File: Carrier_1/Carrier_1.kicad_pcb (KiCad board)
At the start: 2 copper layers, 20 x 32 mm, 3 parts, among them J1 Chubut_2 connector, U1 LGAD_2_pad

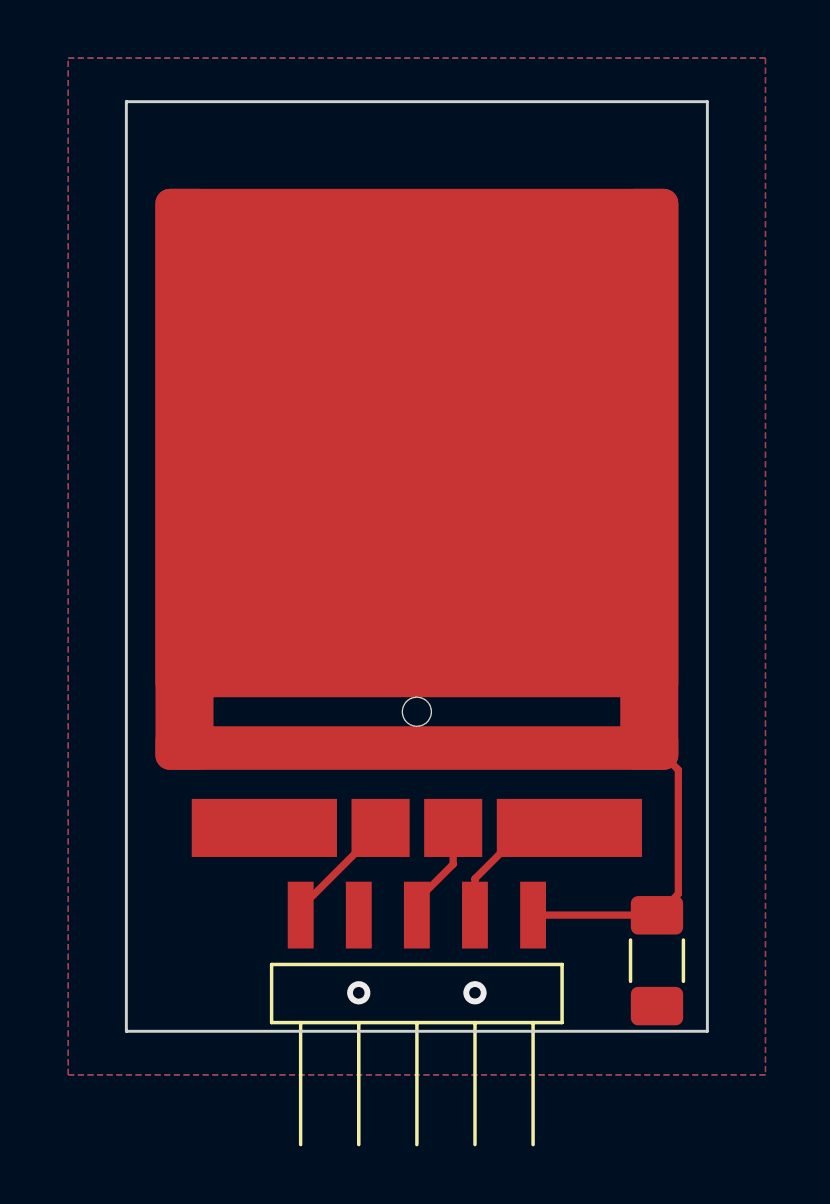
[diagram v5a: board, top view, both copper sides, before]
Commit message: Design with spring loaded pins
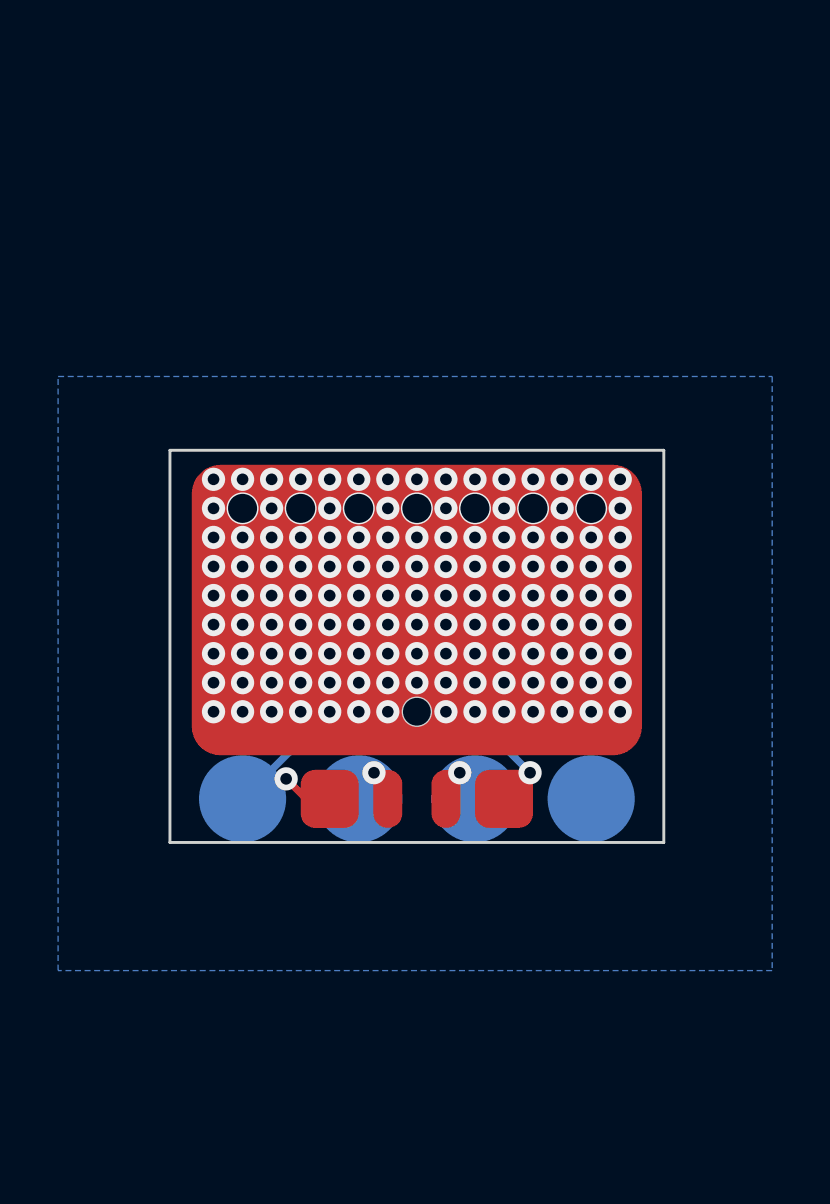
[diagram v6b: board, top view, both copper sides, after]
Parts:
- removed C1: 1n, Capacitor_SMD:C_1206_3216Metric_Pad1.33x1.80mm_HandSolder
- added J2: CH2, chubut:MILL-MAX_0965-0-15-20-80-14-11-0_contact, B.Cu at (2.00, 3.00)
- added J3: HV, chubut:MILL-MAX_0965-0-15-20-80-14-11-0_contact, B.Cu at (6.00, 3.00)
- added J4: GND, chubut:MILL-MAX_0965-0-15-20-80-14-11-0_contact, B.Cu at (-6.00, 3.00)
- J1: value Chubut_2 connector -> CH1; footprint chubut:M22-5330505 -> chubut:MILL-MAX_0965-0-15-20-80-14-11-0_contact; moved to B.Cu
- moved J1 4.47 mm to (-2.00, 3.00), turned to 180 degrees
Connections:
- U1 pad 1: Net-(C1-Pad1) -> /HV
- U1 pad 3: Net-(J1-Pad3) -> Net-(J2-Pad1)
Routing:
- net Net-(C1-Pad1): track 18.9 -> 0.00 mm
- net GND: track 5.22 -> 14.6 mm
- net Net-(J1-Pad3): track 3.52 -> 0.00 mm
- net Net-(J2-Pad1): track 0.00 -> 2.22 mm, vias 0 -> 1
- net Net-(J1-Pad1): track 4.14 -> 2.22 mm, vias 0 -> 1
- net /HV: vias 0 -> 134
- added copper zone on B.Cu, net /HV
- removed copper zone on B.Cu, net GND
- removed copper zone on F.Cu, net GND
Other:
- board size 20 x 32 mm -> 17 x 13.5 mm

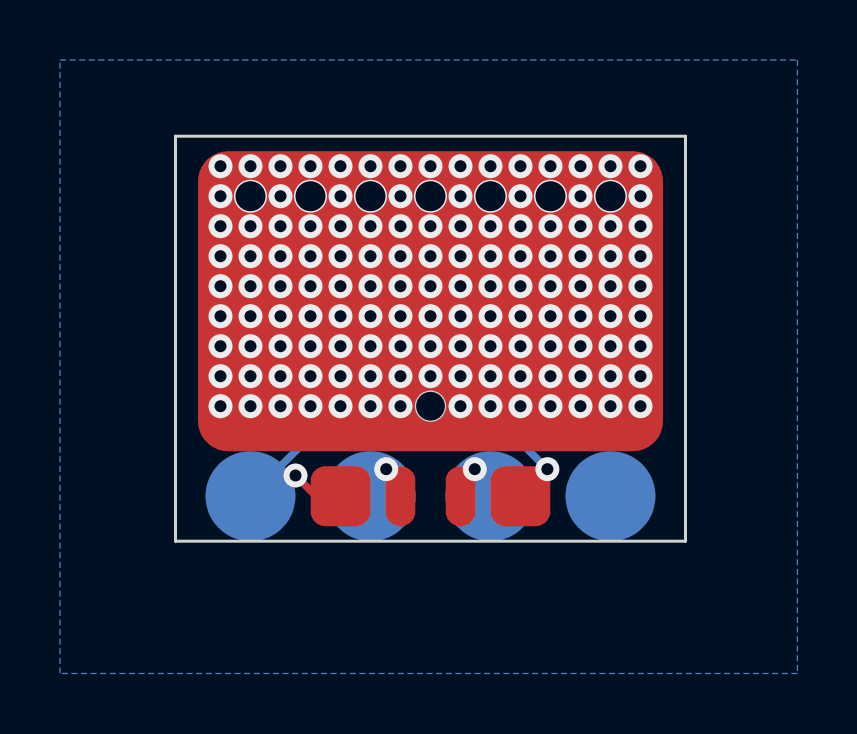
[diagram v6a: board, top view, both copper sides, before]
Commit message: Removed high voltage copper plane on the back side
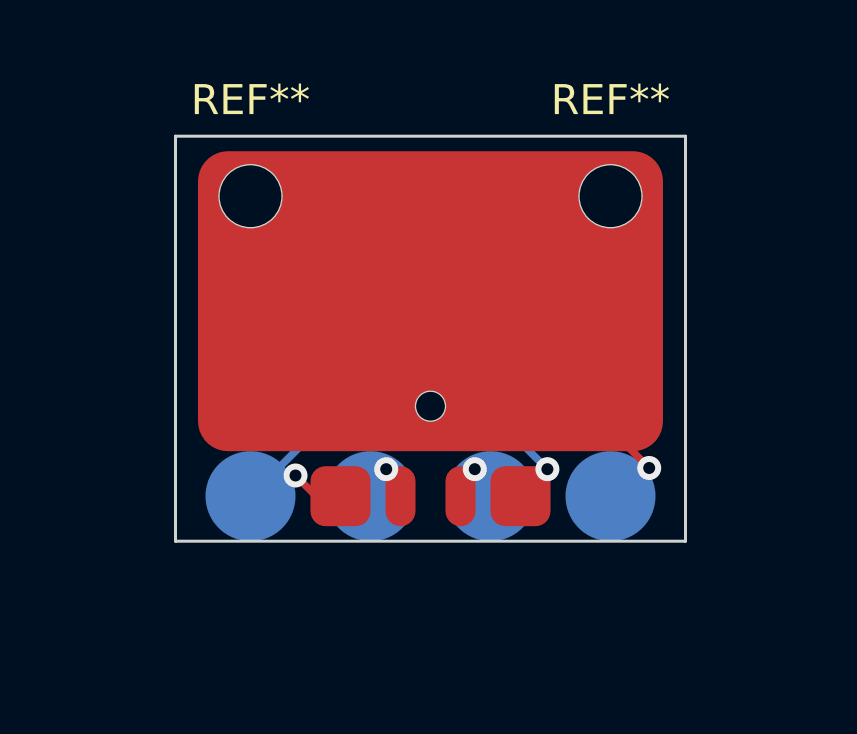
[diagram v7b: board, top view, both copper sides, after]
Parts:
- added REF**: MountingHole_2.1mm, MountingHole:MountingHole_2.1mm, F.Cu at (6.00, -7.00)
- added REF**: MountingHole_2.1mm, MountingHole:MountingHole_2.1mm, F.Cu at (-6.00, -7.00)
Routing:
- net /HV: track 0.00 -> 11.3 mm, vias 134 -> 1
- removed copper zone on B.Cu, net /HV

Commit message: Carrier ready
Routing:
- net /HV: vias 1 -> 31
- added copper zone on B.Cu, net /HV
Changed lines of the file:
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@@
     (tags "mounting hole 2.1mm no annular")
     (attr exclude_from_pos_files exclude_from_bom)
-    (fp_text reference "REF**" (at 0 -3.2) (layer "F.SilkS")
+    (fp_text reference "REF**" (at 0 -3.2) (layer "F.SilkS") hide
       (effects (font (size 1 1) (thickness 0.15)))
     )
@@
     (tags "mounting hole 2.1mm no annular")
     (attr exclude_from_pos_files exclude_from_bom)
-    (fp_text reference "REF**" (at 0 -3.2) (layer "F.SilkS")
+    (fp_text reference "REF**" (at 0 -3.2) (layer "F.SilkS") hide
       (effects (font (size 1 1) (thickness 0.15)))
     )
@@
       (effects (font (size 1 1) (thickness 0.15)) (justify mirror))
     )
-    (pad "1" smd circle (at 0 0 180) (size 3 3) (layers "B.Cu" "B.Mask")
+    (pad "1" smd circle (at 0 0 180) (size 2 2) (layers "B.Cu" "B.Mask")
       (net 3 "Net-(J1-Pad1)") (pinfunction "Pin_1") (pintype "passive"))
   )
@@
       (effects (font (size 1 1) (thickness 0.15)) (justify mirror))
     )
-    (pad "1" smd circle (at 0 0 180) (size 3 3) (layers "B.Cu" "B.Mask")
+    (pad "1" smd circle (at 0 0 180) (size 2 2) (layers "B.Cu" "B.Mask")
       (net 2 "Net-(J2-Pad1)") (pinfunction "Pin_1") (pintype "passive"))
   )
@@
       (effects (font (size 1 1) (thickness 0.15)) (justify mirror))
     )
-    (pad "1" smd circle (at 0 0 180) (size 3 3) (layers "B.Cu" "B.Mask")
+    (pad "1" smd circle (at 0 0 180) (size 2 2) (layers "B.Cu" "B.Mask")
       (net 1 "GND") (pinfunction "Pin_1") (pintype "passive"))
   )
@@
       (effects (font (size 1 1) (thickness 0.15)) (justify mirror))
     )
-    (pad "1" smd circle (at 0 0 180) (size 3 3) (layers "B.Cu" "B.Mask")
+    (pad "1" smd circle (at 0 0 180) (size 2 2) (layers "B.Cu" "B.Mask")
       (net 4 "/HV") (pinfunction "Pin_1") (pintype "passive"))
   )
@@
   (segment (start 1.73 -3.5) (end 0 -3.5) (width 0.25) (layer "F.Cu") (net 4))
   (segment (start 7.29 2.06) (end 1.73 -3.5) (width 0.25) (layer "F.Cu") (net 4))
+  (via (at -4 -6) (size 0.8) (drill 0.4) (layers "F.Cu" "B.Cu") (net 4))
+  (via (at 2 -6) (size 0.8) (drill 0.4) (layers "F.Cu" "B.Cu") (net 4))
+  (via (at 2 -8) (size 0.8) (drill 0.4) (layers "F.Cu" "B.Cu") (net 4))
+  (via (at 4 -6) (size 0.8) (drill 0.4) (layers "F.Cu" "B.Cu") (net 4))
+  (via (at -6 -2) (size 0.8) (drill 0.4) (layers "F.Cu" "B.Cu") (net 4))
+  (via (at 2 0) (size 0.8) (drill 0.4) (layers "F.Cu" "B.Cu") (net 4))
+  (via (at -2 -2) (size 0.8) (drill 0.4) (layers "F.Cu" "B.Cu") (net 4))
+  (via (at 6 -4) (size 0.8) (drill 0.4) (layers "F.Cu" "B.Cu") (net 4))
+  (via (at 0 -2) (size 0.8) (drill 0.4) (layers "F.Cu" "B.Cu") (net 4))
+  (via (at -2 0) (size 0.8) (drill 0.4) (layers "F.Cu" "B.Cu") (net 4))
+  (via (at 2 -2) (size 0.8) (drill 0.4) (layers "F.Cu" "B.Cu") (net 4))
+  (via (at 6 0) (size 0.8) (drill 0.4) (layers "F.Cu" "B.Cu") (net 4))
+  (via (at 4 -4) (size 0.8) (drill 0.4) (layers "F.Cu" "B.Cu") (net 4))
+  (via (at -6 -4) (size 0.8) (drill 0.4) (layers "F.Cu" "B.Cu") (net 4))
+  (via (at 0 -6) (size 0.8) (drill 0.4) (layers "F.Cu" "B.Cu") (net 4))
   (via (at 7.29 2.06) (size 0.8) (drill 0.4) (layers "F.Cu" "B.Cu") (net 4))
+  (via (at 0 -8) (size 0.8) (drill 0.4) (layers "F.Cu" "B.Cu") (net 4))
+  (via (at -4 -2) (size 0.8) (drill 0.4) (layers "F.Cu" "B.Cu") (net 4))
+  (via (at 6 -2) (size 0.8) (drill 0.4) (layers "F.Cu" "B.Cu") (net 4))
+  (via (at -6 0) (size 0.8) (drill 0.4) (layers "F.Cu" "B.Cu") (net 4))
+  (via (at -2 -6) (size 0.8) (drill 0.4) (layers "F.Cu" "B.Cu") (net 4))
+  (via (at 4 0) (size 0.8) (drill 0.4) (layers "F.Cu" "B.Cu") (net 4))
+  (via (at 4 -8) (size 0.8) (drill 0.4) (layers "F.Cu" "B.Cu") (net 4))
+  (via (at 4 -2) (size 0.8) (drill 0.4) (layers "F.Cu" "B.Cu") (net 4))
+  (via (at 0 -4) (size 0.8) (drill 0.4) (layers "F.Cu" "B.Cu") (net 4))
+  (via (at -2 -8) (size 0.8) (drill 0.4) (layers "F.Cu" "B.Cu") (net 4))
+  (via (at -2 -4) (size 0.8) (drill 0.4) (layers "F.Cu" "B.Cu") (net 4))
+  (via (at 2 -4) (size 0.8) (drill 0.4) (layers "F.Cu" "B.Cu") (net 4))
+  (via (at -4 0) (size 0.8) (drill 0.4) (layers "F.Cu" "B.Cu") (net 4))
+  (via (at -4 -8) (size 0.8) (drill 0.4) (layers "F.Cu" "B.Cu") (net 4))
+  (via (at -4 -4) (size 0.8) (drill 0.4) (layers "F.Cu" "B.Cu") (net 4))
   (segment (start 6.35 3) (end 7.29 2.06) (width 0.25) (layer "B.Cu") (net 4))
   (segment (start 6 3) (end 6.35 3) (width 0.25) (layer "B.Cu") (net 4))
-  (zone (net 0) (net_name "") (layers *.Adhes *.Paste *.SilkS *.Mask) (hatch edge 0.508)
-    (connect_pads (clearance 0))
-    (min_thickness 0.254)
-    (keepout (tracks not_allowed) (vias not_allowed) (pads not_allowed) (copperpour allowed) (footprints allowed))
-    (fill (thermal_gap 0.508) (thermal_bridge_width 0.508))
+  (zone (net 4) (net_name "/HV") (layer "B.Cu") (hatch edge 0.508)
+    (connect_pads (clearance 0.508))
+    (min_thickness 0.254) (filled_areas_thickness no)
+    (fill yes (thermal_gap 0.508) (thermal_bridge_width 0.508))
     (polygon
       (pts
-        (xy 11.19 6.67)
-        (xy -10.48 6.67)
-        (xy -10.48 -10.32)
-        (xy 11.19 -10.32)
+        (xy 10.3 6.34)
+        (xy -10.18 6.34)
+        (xy -10.18 -10.32)
+        (xy 10.3 -10.32)
       )
     )
